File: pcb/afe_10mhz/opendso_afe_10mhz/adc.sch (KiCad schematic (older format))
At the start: 18 parts, among them IC22 MAX19506

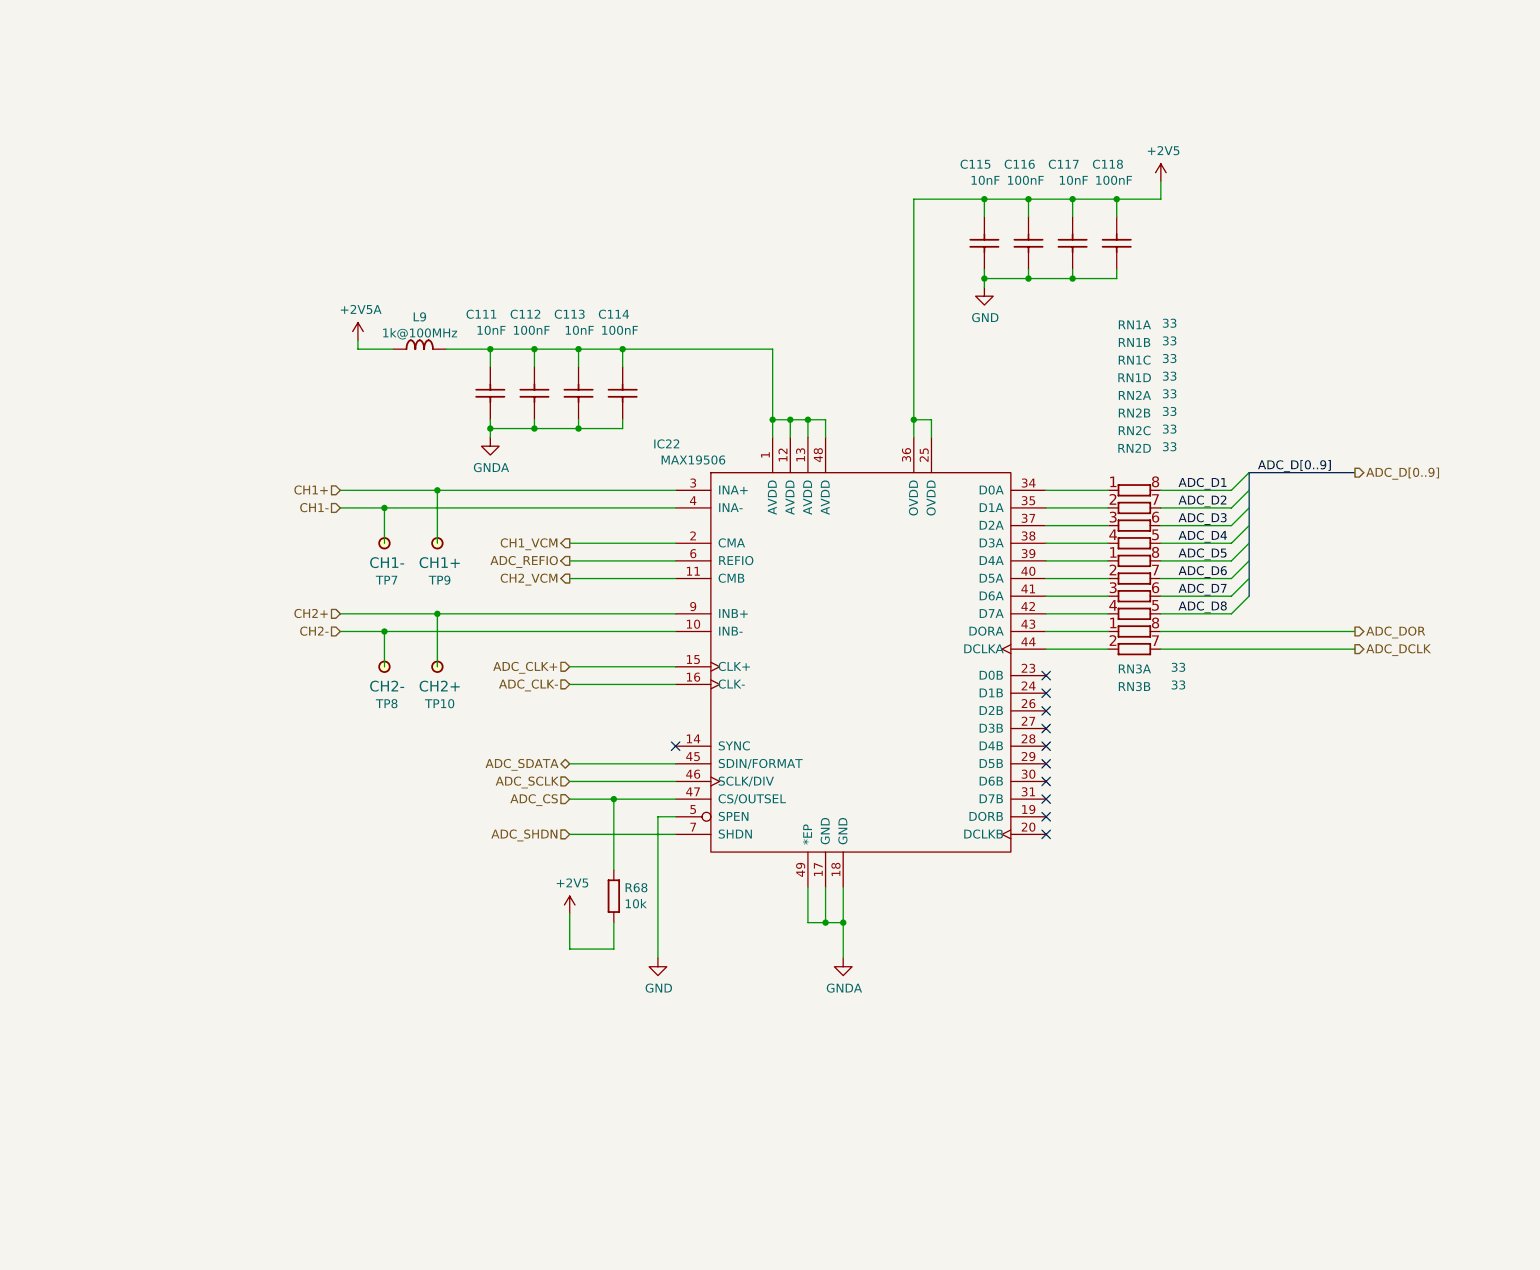
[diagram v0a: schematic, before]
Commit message: AFE schematic: finished port to KiCad
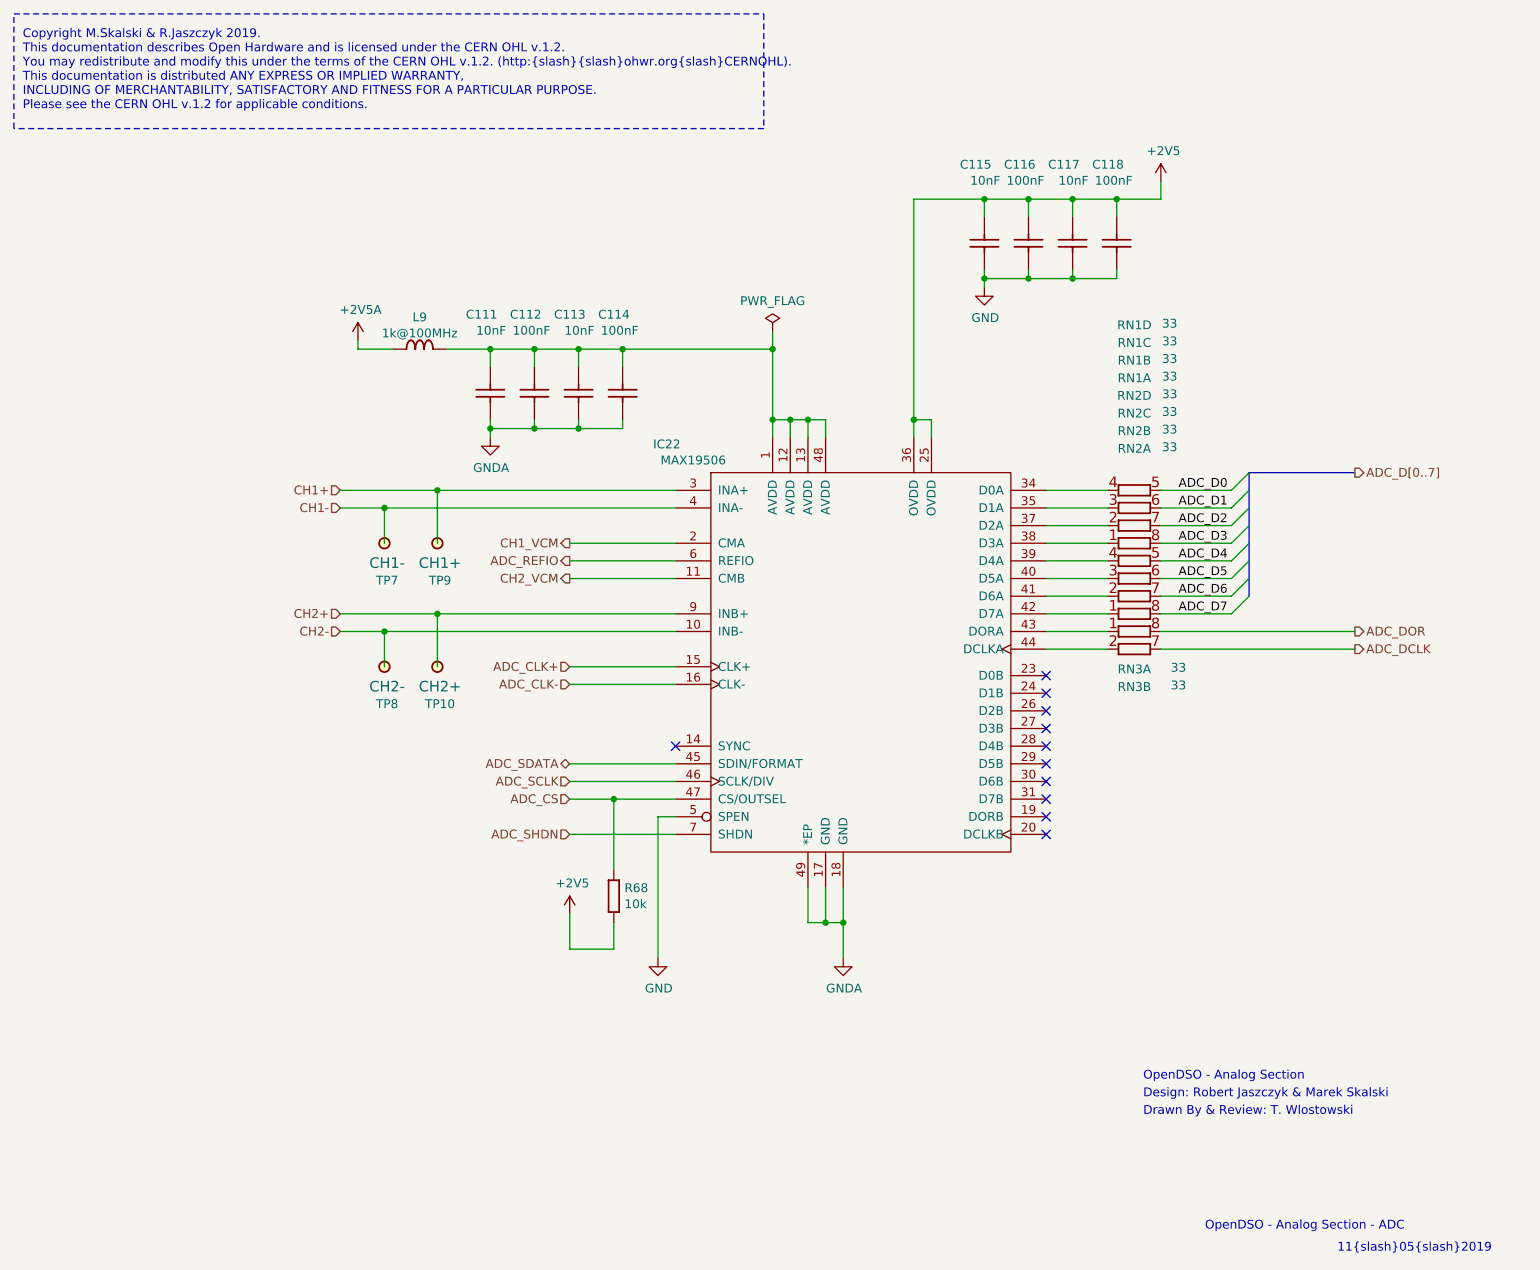
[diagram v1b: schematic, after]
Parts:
- C111, C112, C113, C114, C115, C116, C117, C118: footprint CAPC1608X87N -> Capacitors SMD:CAPC1608X87N
- TP10, TP7, TP8, TP9: footprint TPS127 -> Pads:TPS127
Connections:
- net ADC_D8 is gone; now on net ADC_D4: RN2.5
- net ADC_D1: now also RN1.6; no longer RN1.8
- net ADC_D3: now also RN1.8; no longer RN1.6
- net ADC_D4: no longer RN1.5
- net ADC_D5: now also RN2.6; no longer RN2.8
- net ADC_D7: now also RN2.8; no longer RN2.6
- net at IC22.34 (D0A): now also RN1.4; no longer RN1.1
- net at IC22.35 (D1A): now also RN1.3; no longer RN1.2
- net at IC22.37 (D2A): now also RN1.2; no longer RN1.3
- net at IC22.38 (D3A): now also RN1.1; no longer RN1.4
- net at IC22.39 (D4A): now also RN2.4; no longer RN2.1
- net at IC22.40 (D5A): now also RN2.3; no longer RN2.2
- net at IC22.41 (D6A): now also RN2.2; no longer RN2.3
- net at IC22.42 (D7A): now also RN2.1; no longer RN2.4
- new net ADC_D0: RN1.5
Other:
- note added: "11/05/2019\n"
- note added: "Copyright M.Skalski & R.Jaszczyk 2019.\nThis documentation describes Open Hardware and is licensed under the CERN OHL v.1.2.\nYou may redistribute and modify this under the terms of the CERN OHL v.1.2. (http://ohwr.org/CERNOHL).\nThis documentation is distributed ANY EXPRESS OR IMPLIED WARRANTY,\nINCLUDING OF MERCHANTABILITY, SATISFACTORY AND FITNESS FOR A PARTICULAR PURPOSE.\nP…"
- note added: "Design: Robert Jaszczyk & Marek Skalski\n"
- note added: "Drawn By & Review: T. Wlostowski\n"
- note added: "OpenDSO - Analog Section - ADC\n"
- note added: "OpenDSO - Analog Section\n"
- moved on the sheet: RN1A, RN1B, RN1C, RN1D, RN2A, RN2B, RN2C, RN2D
